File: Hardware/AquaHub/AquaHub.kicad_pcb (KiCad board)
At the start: 2 copper layers, 184 x 119 mm, 99 parts, among them J1 Screw_Terminal_01x02, J10 PinHeader6, J11 Power_Conn, J13 PinHeader2, J14 PinHeader3, J2 Screw_Terminal_01x02, J3 Screw_Terminal_01x02, J4 Screw_Terminal_01x02, J5 Screw_Terminal_01x02, J6 Screw_Terminal_01x02, J7 Control_Conn, J8 Screw_Terminal_01x02, K1 5A Relay, K2 5A Relay, K3 5A Relay, K4 5A Relay, K5 5A Relay, K6 5A Relay, Q2 2SC1815, SW1 SW_Push, SW2 SW_Push, SW3 SW_Push, SW4 SW_Push, SW5 SW_Push, SW6 SW_Push, U1 ESP32-WROOM, U2 Current Sense, U3 1A 3.3V, U4 Low-Side Driver, U5 1A 5V, U6 TCA9534, U7 DS1307+, U8 TPIC2810D, Y1 32.768KHz

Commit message: Commit latest hardware updates and initial firmware
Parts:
- BT1: footprint AquaFootprints:Multicomp-BC-2001 -> Battery:BatteryHolder_Multicomp_BC-2001_1x2032
- moved BT1 13.0 mm to (220.9, 43.5)
- moved C1 6.65 mm to (204.2, 100.6)
- moved C2 6.65 mm to (204.2, 105.7)
- moved R1 6.65 mm to (204.2, 103.2)
- moved U2 6.65 mm to (204.6, 111.9)
- moved J14 1.89 mm to (205.9, 38.0)
- renumbered J8 to J7, J7 to J8
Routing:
- net /PowerBoard/LIVE: track 150.9 -> 155.9 mm
- net /Temp_Sense: track 31.0 -> 34.7 mm
- net +5V: track 458.4 -> 460.3 mm
- net Power_Sense: track 71.9 -> 70.3 mm
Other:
- net class MainsRails: trace_width 2 -> 2.5
- board text added: "AquaHub ControlBoard v2.0"
- board text added: "AquaHub PowerBoard v2.0"
- board text removed: "AquaHub ControlBoard v1.0"
- board text removed: "AquaHub PowerBoard v1.0"

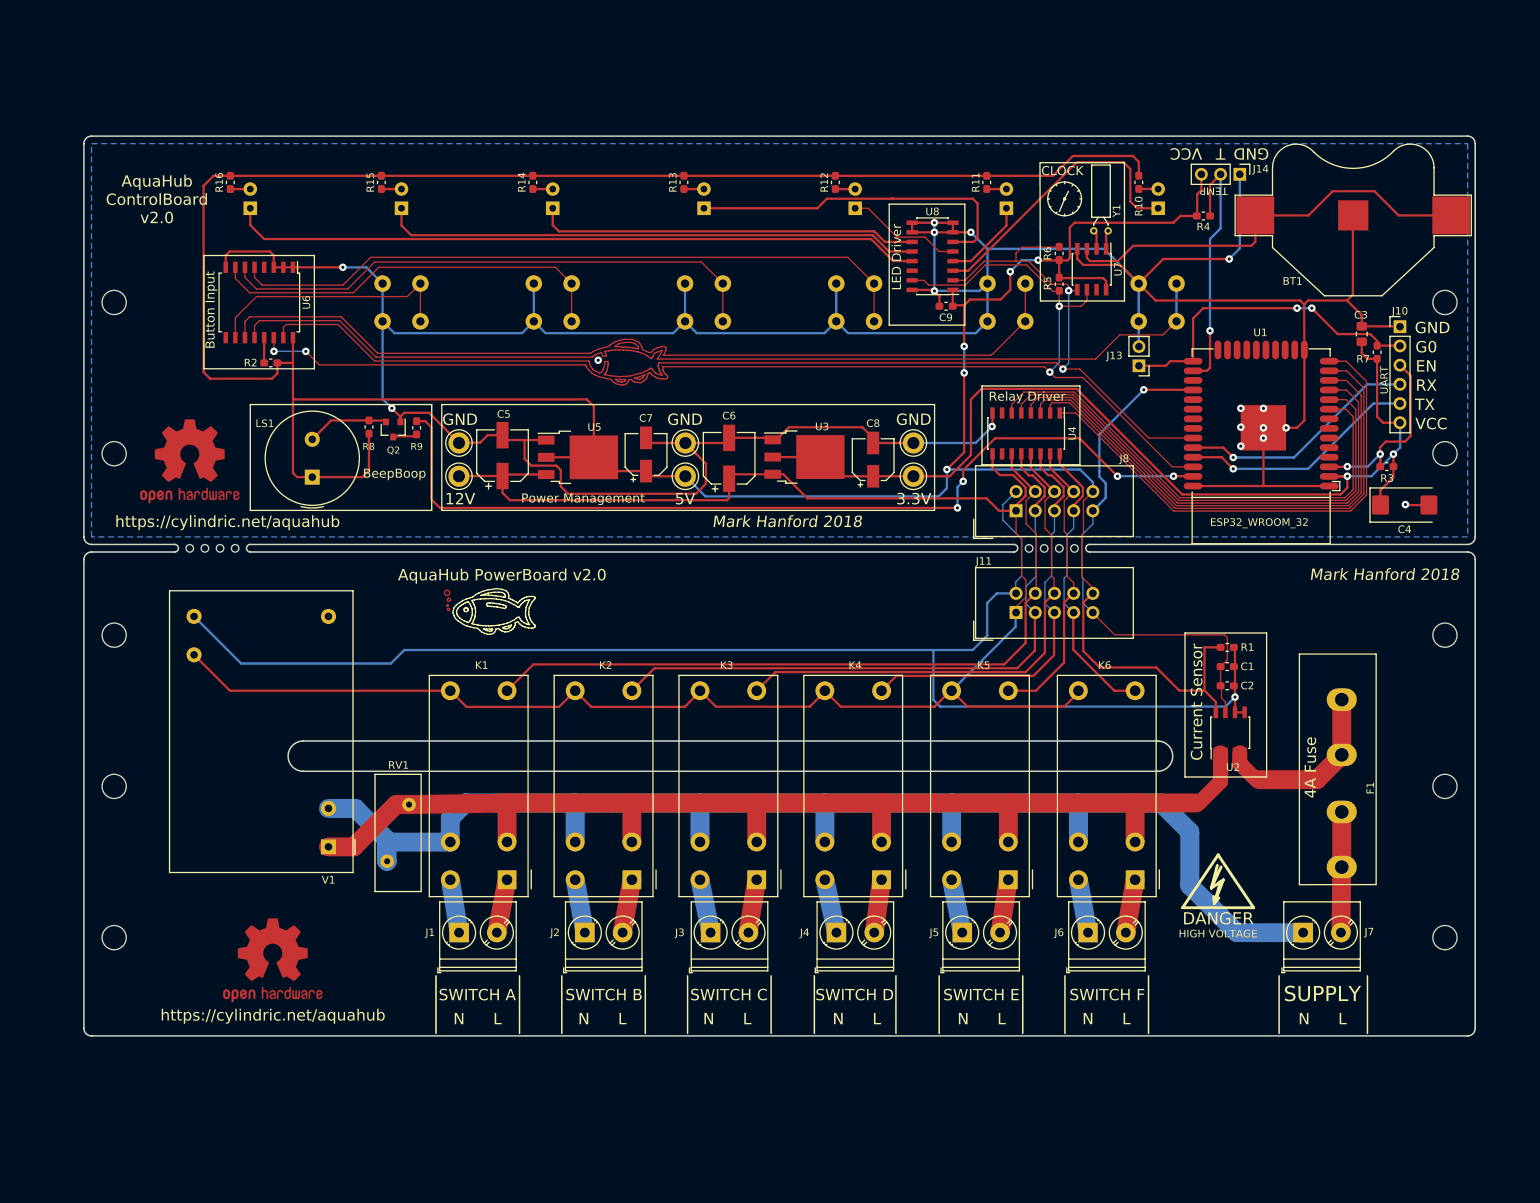
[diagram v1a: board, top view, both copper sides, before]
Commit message: Big PCB switch to a single board. Again.
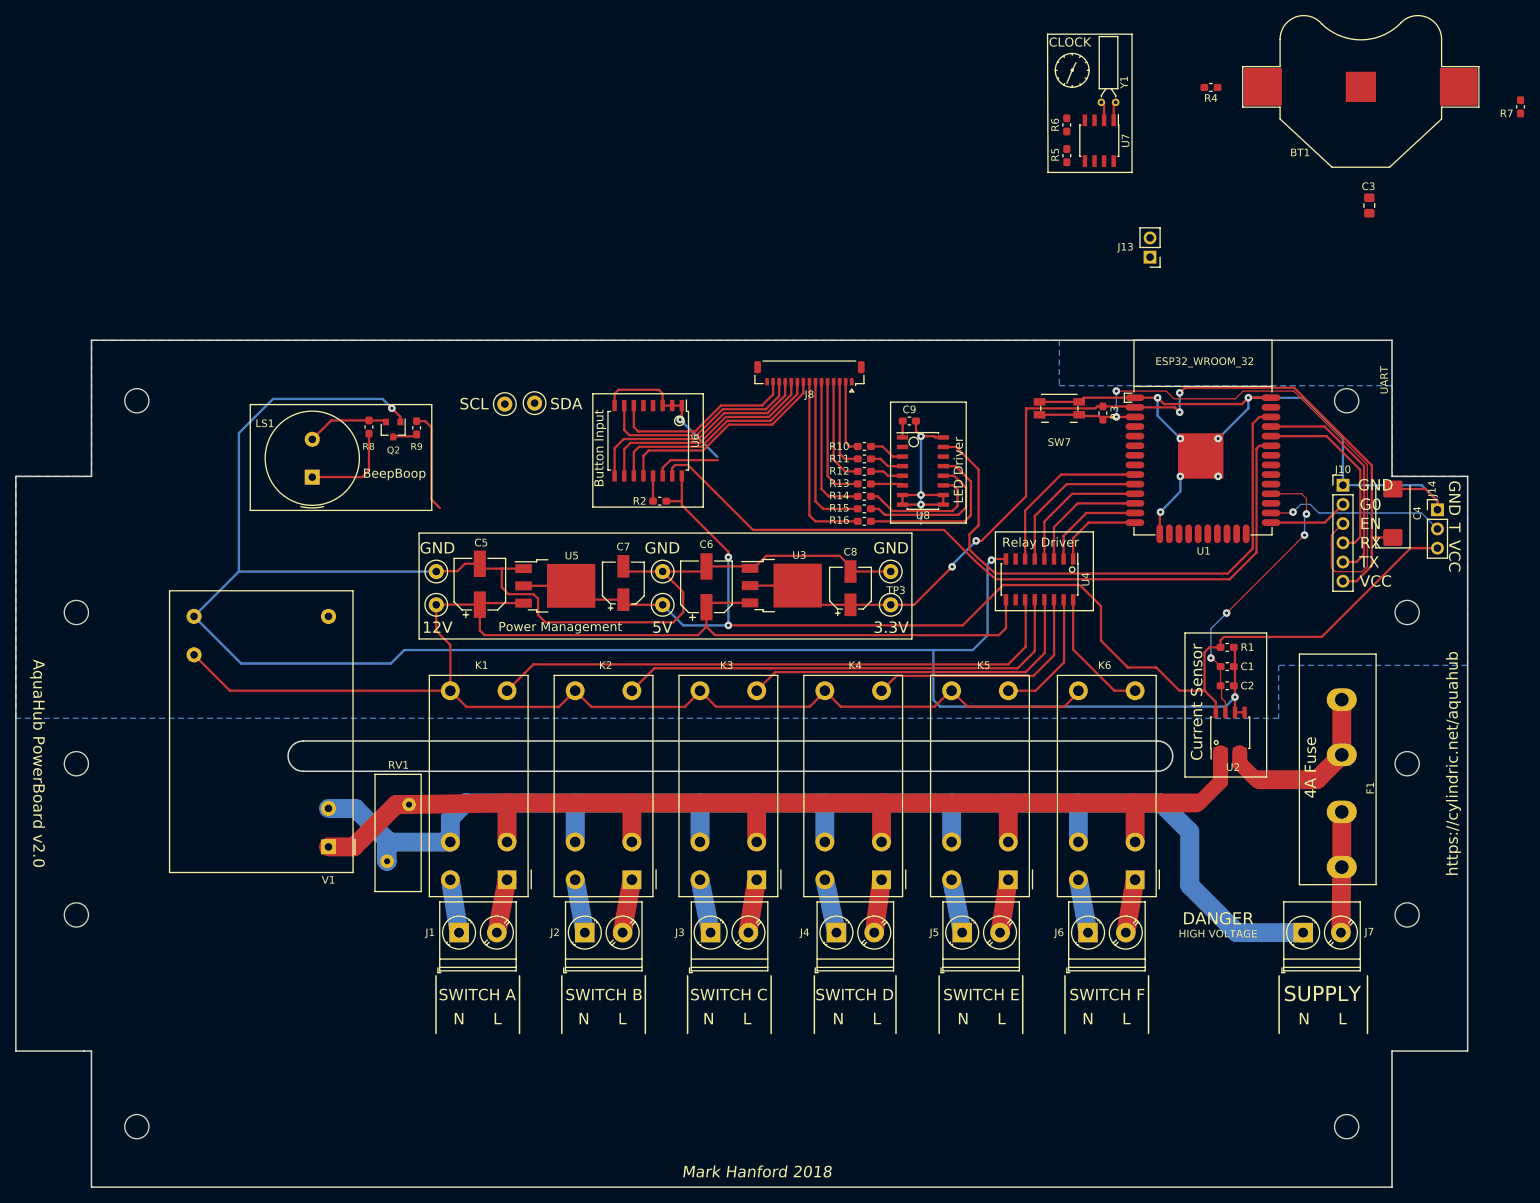
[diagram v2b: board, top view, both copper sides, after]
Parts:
- removed D1, D2, D3, D4, D5, D6, D7: LED, LED_THT:LED_D5.0mm
- removed H11, H12, H13, H14, H15, H16, H17, H18: MountingHole, AquaFootprints:Breakaway 1mm
- removed J11: Power_Conn, Connector_IDC:IDC-Header_2x05_P2.54mm_Vertical
- removed REF**: Symbol_HighVoltage_Type2_CopperTop_VerySmall, Symbol:Symbol_HighVoltage_Type2_CopperTop_VerySmall
- removed REF**: Fish, AquaFootprints:Fish
- removed REF** (x2): OSHW-Logo2_14.6x12mm_Copper, Symbol:OSHW-Logo2_14.6x12mm_Copper
- removed SW1, SW2, SW3, SW4, SW5, SW6: SW_Push, Button_Switch_THT:SW_CK_D6R_SPST_12mm_H14.3mm
- added SW7: Reset, Button_Switch_SMD:Panasonic_EVQPUJ_EVQPUA, F.Cu at (182.0, 69.0)
- added TP7: TEST_SCL, TestPoint:TestPoint_Loop_D2.50mm_Drill1.0mm, F.Cu at (108.7, 68.4)
- added TP8: TEST_SDA, TestPoint:TestPoint_Loop_D2.50mm_Drill1.0mm, F.Cu at (112.6, 68.3)
- J8: value Control_Conn -> Conn_01x15_Female; footprint Connector_IDC:IDC-Header_2x05_P2.54mm_Vertical -> Connector_Hirose:Hirose_DF52-15S-0.8H_1x15-1MP_P0.80mm_Horizontal
- TP1, TP2, TP3, TP4, TP5, TP6: footprint TestPoint:TestPoint_Keystone_5010-5014_Multipurpose -> TestPoint:TestPoint_Loop_D2.50mm_Drill1.0mm
- moved R16 95.1 mm to (156.2, 83.9), turned to 180 degrees
- moved R15 77.1 mm to (156.2, 82.3), turned to 180 degrees
- moved R14 60.4 mm to (156.2, 80.6), turned to 180 degrees
- moved R2 54.6 mm to (129.1, 81.3)
- moved U6 54.6 mm to (127.6, 73.3)
- moved J14 51.5 mm to (232.0, 82.4), turned to 0 degrees
- moved H2 51.1 mm to (60.0, 68.0)
- moved R10 50.4 mm to (156.2, 74.0), turned to 180 degrees
- moved R13 46.5 mm to (156.2, 79.0), turned to 180 degrees
- moved H7 41.3 mm to (52.0, 96.0)
- moved H8 41.3 mm to (52.0, 116.0)
- moved R11 40.0 mm to (156.2, 75.7), turned to 180 degrees
- moved R12 38.4 mm to (156.2, 77.3), turned to 180 degrees
- moved R3 38.2 mm to (187.8, 69.6), turned to 270 degrees
- moved R7 37.6 mm to (243.0, 29.1)
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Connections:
- J8 pad 1: +12V -> +5V
- J8 pad 10: +5V -> SW_2
- J8 pad 2: GND -> LED_1
- J8 pad 3: RE2 -> LED_2
- J8 pad 4: RE1 -> LED_3
- J8 pad 5: RE4 -> LED_4
- J8 pad 6: RE3 -> LED_5
- J8 pad 7: RE6 -> LED_6
- J8 pad 8: RE5 -> LED_7
- J8 pad 9: Power_Sense -> SW_1
- R10 pad 1: Net-(D1-Pad2) -> Net-(R10-Pad1)
- R10 pad 2: +5V -> LED_1
- R11 pad 1: Net-(D2-Pad2) -> Net-(R11-Pad1)
- R11 pad 2: +5V -> LED_2
- R12 pad 1: Net-(D3-Pad2) -> Net-(R12-Pad1)
- R12 pad 2: +5V -> LED_3
- R13 pad 1: Net-(D4-Pad2) -> Net-(R13-Pad1)
- R13 pad 2: +5V -> LED_4
- R14 pad 1: Net-(D5-Pad2) -> Net-(R14-Pad1)
- R14 pad 2: +5V -> LED_5
- R15 pad 1: Net-(D6-Pad2) -> Net-(R15-Pad1)
- R15 pad 2: +5V -> LED_6
- R16 pad 1: Net-(D7-Pad2) -> Net-(R16-Pad1)
- R16 pad 2: +5V -> LED_7
- U6 pad 10: Net-(SW6-Pad1) -> SW_3
- U6 pad 11: Net-(SW2-Pad1) -> SW_2
- U6 pad 12: Net-(SW1-Pad1) -> SW_1
- U6 pad 6: Net-(SW4-Pad1) -> SW_6
- U6 pad 7: Net-(SW5-Pad1) -> SW_5
- U6 pad 9: Net-(U6-Pad9) -> SW_4
- U8 pad 11: Net-(D5-Pad1) -> Net-(R14-Pad1)
- U8 pad 12: Net-(D6-Pad1) -> Net-(R15-Pad1)
- U8 pad 13: Net-(D7-Pad1) -> Net-(R16-Pad1)
- U8 pad 3: Net-(D1-Pad1) -> Net-(R10-Pad1)
- U8 pad 4: Net-(D2-Pad1) -> Net-(R11-Pad1)
- U8 pad 5: Net-(D3-Pad1) -> Net-(R12-Pad1)
- U8 pad 6: Net-(D4-Pad1) -> Net-(R13-Pad1)
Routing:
- net +5V: track 460.3 -> 188.7 mm, vias 5 -> 2
- net GND: track 661.3 -> 511.8 mm, vias 18 -> 14
- net Net-(SW1-Pad1): track 137.1 -> 0.00 mm
- net Net-(SW2-Pad1): track 117.4 -> 0.00 mm
- net /Sounder: track 121.4 -> 13.4 mm, vias 4 -> 0
- net Net-(D7-Pad1): track 91.7 -> 0.00 mm
- net Net-(U6-Pad5): track 91.7 -> 0.00 mm
- net SCL: track 173.3 -> 85.1 mm, vias 4 -> 0
- net Net-(SW4-Pad1): track 72.8 -> 0.00 mm
- net Net-(D6-Pad1): track 71.2 -> 0.00 mm
- net SDA: track 172.5 -> 102.1 mm, vias 2 -> 0
- net +BATT: track 56.8 -> 0.00 mm
- net /POW6: track 67.9 -> 11.8 mm
- net /POW5: track 68.8 -> 13.7 mm
- net Net-(SW5-Pad1): track 54.0 -> 0.00 mm
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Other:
- board size 184 x 119 mm -> 192 x 112 mm
- board text added: "SCL"
- board text added: "SDA"
- board text removed: "AquaHub ControlBoard v2.0"
- board text removed: "TEMP"

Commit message: Finalising the Rev2 hardware.
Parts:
- removed H10, H9: MountingHole, MountingHole:MountingHole_3.2mm_M3
- removed J13: PinHeader2, Connector_PinHeader_2.54mm:PinHeader_1x02_P2.54mm_Vertical
- removed TP5: Test_12V_GND, TestPoint:TestPoint_Loop_D2.50mm_Drill1.0mm
- removed TP6: TEST_5V_GND, TestPoint:TestPoint_Loop_D2.50mm_Drill1.0mm
- added C10: 0.1uF, Capacitor_SMD:C_0805_2012Metric_Pad1.15x1.40mm_HandSolder, F.Cu at (189.5, 42.5)
- added C11: 0.1uF, Capacitor_SMD:C_0805_2012Metric_Pad1.15x1.40mm_HandSolder, F.Cu at (201.8, 67.2)
- added R17: 1.5k, Resistor_SMD:R_0603_1608Metric_Pad1.05x0.95mm_HandSolder, F.Cu at (209.8, 67.3)
- added U9: PCT2075, Package_SO:TSOP-6_1.65x3.05mm_P0.95mm, F.Cu at (205.8, 67.2)
- C4: value 100uF -> 0.1uF; footprint Capacitor_Tantalum_SMD:CP_EIA-7343-31_Kemet-D_Pad2.25x2.55mm_HandSolder -> Capacitor_SMD:C_0805_2012Metric_Pad1.15x1.40mm_HandSolder
- F1: footprint AquaFootprints:Fuse_Clip_5mm -> Fuse:Fuseholder_Glass_5mmx20mm
- J8: footprint Connector_Hirose:Hirose_DF52-15S-0.8H_1x15-1MP_P0.80mm_Horizontal -> Connector_PinHeader_2.00mm:PinHeader_2x08_P2.00mm_Vertical
- Q2: value 2SC1815 -> 2SC4738; footprint Package_TO_SOT_SMD:SOT-23 -> Package_TO_SOT_SMD:SOT-416
- SW7: footprint Button_Switch_SMD:Panasonic_EVQPUJ_EVQPUA -> Button_Switch_SMD:SW_SPST_PTS645
- TP1: value TEST_5V -> TEST_5V_GND
- TP3: value Test_3V3_GND -> TEST_5V
- U1: footprint Module:Espressif_ESP32_WROOM_32_SMT -> Module:Espressif_ESP32_WROOM_32D_SMT
- U2: value Current Sense -> MLX91210
- U4: value Low-Side Driver -> TPL7407LADR
- Y1: footprint Crystal:Crystal_C26-LF_D2.1mm_L6.5mm_Horizontal -> Crystal:Crystal_SMD_SeikoEpson_MC146-4Pin_6.7x1.5mm_HandSoldering
- moved H1 206.5 mm to (228.0, 44.0)
- moved BT1 140.1 mm to (84.5, 54.0)
- moved H4 100.3 mm to (236.0, 65.0)
- moved TP4 81.2 mm to (176.1, 68.0)
- moved Y1 76.7 mm to (115.7, 49.3)
- moved U7 64.2 mm to (125.4, 50.6), turned to 0 degrees
- moved TP7 63.6 mm to (172.1, 63.9)
- moved J10 62.3 mm to (174.0, 36.6), turned to 90 degrees
- moved TP8 55.6 mm to (168.0, 63.9)
- moved R7 50.7 mm to (195.7, 47.3)
- moved R6 46.3 mm to (215.1, 64.9), turned to 0 degrees
- moved TP1 43.7 mm to (164.0, 68.0)
- moved R4 42.6 mm to (225.0, 62.4)
- moved R5 42.1 mm to (215.1, 62.9), turned to 180 degrees
- moved LS1 38.5 mm to (103.0, 45.1)
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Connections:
- SW7 pad 2: GND -> Net-(C10-Pad1)
- TP1 pad 1: +5V -> GND
- TP3 pad 1: GND -> +5V
- Y1 pad 2: Net-(U7-Pad2) -> Net-(Y1-Pad2)
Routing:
- net /Sounder: track 13.4 -> 119.9 mm, vias 0 -> 2
- net +5V: track 188.7 -> 278.0 mm, vias 2 -> 8
- net SCL: track 85.1 -> 160.5 mm, vias 0 -> 5
- net +BATT: track 0.00 -> 56.3 mm
- net SDA: track 102.1 -> 157.3 mm, vias 0 -> 8
- net /IO0: track 10.5 -> 65.5 mm, vias 0 -> 4
- net /EN: track 80.1 -> 31.0 mm, vias 2 -> 0
- net /RX: track 25.1 -> 49.6 mm
- net GND: track 511.8 -> 496.7 mm, vias 14 -> 20
- net /TX: track 29.4 -> 43.9 mm
- net Net-(C10-Pad1): track 0.00 -> 13.9 mm
- net /POW1: track 22.9 -> 34.7 mm
- net /POW2: track 20.7 -> 32.0 mm
- net RE5: track 17.2 -> 27.7 mm
- net RE4: track 32.1 -> 42.3 mm
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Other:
- board size 192 x 112 mm -> 190 x 90 mm
- net class Power added: clearance 0.2, trace_width 0.508, via_dia 1, via_drill 0.4
- board text added: "Temp"
- board text removed: "BeepBoop"
- board text removed: "SUPPLY"
- board text removed: "SWITCH A"
- board text removed: "SWITCH B"
- board text removed: "SWITCH C"
- board text removed: "SWITCH D"
- board text removed: "SWITCH E"
- board text removed: "SWITCH F"
